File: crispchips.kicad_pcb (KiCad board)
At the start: 2 copper layers, 113 parts, among them IC1 ISL85003FRZ, IC2 ISL9307IRTAANFZ-T7A, IC3 ESP32-S2-MINI-1-N4R2, IC4 XC3S250E-4VQG100C, IC5 PCA9306DCUR, IC6 W25N512GVEIG, J2 Conn_01x02_Male, J3 Conn_01x04, J4 JTAG, J5 HDMI_A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

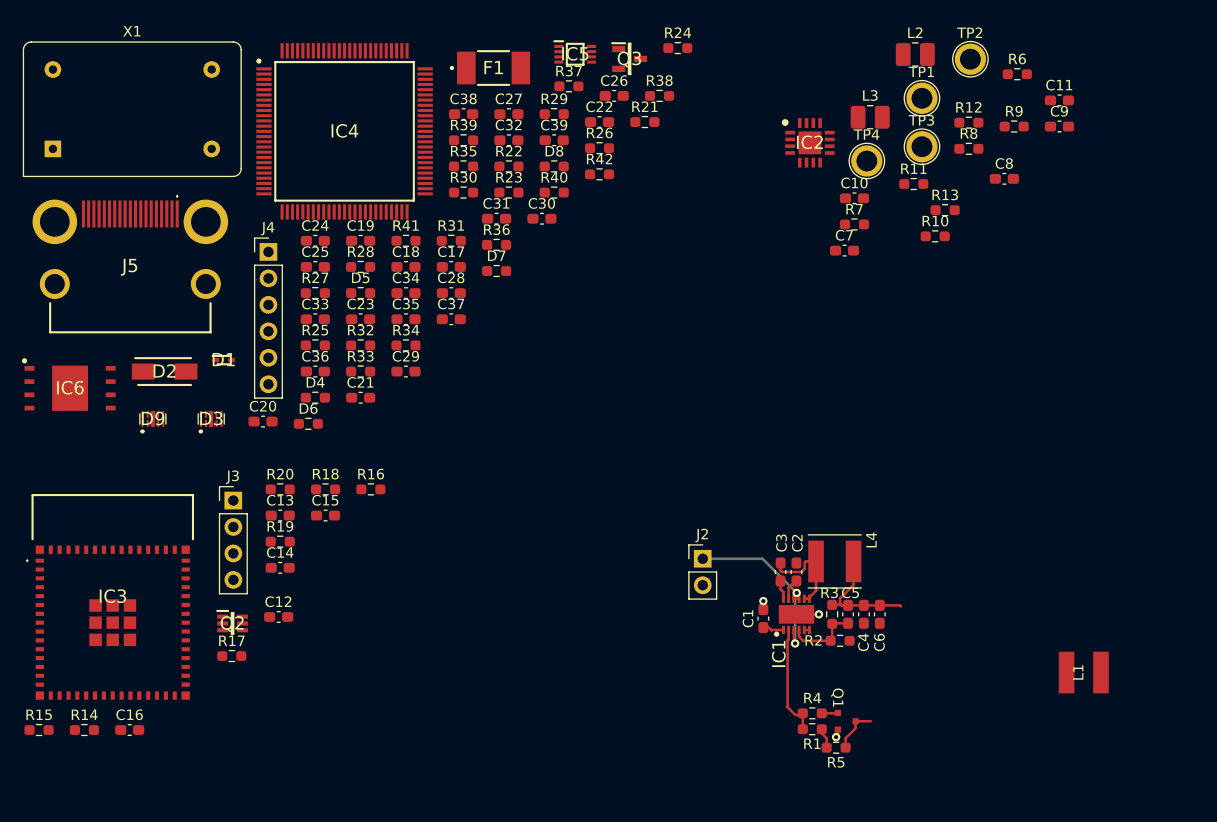
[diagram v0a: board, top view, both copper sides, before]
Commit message: supply layout review step
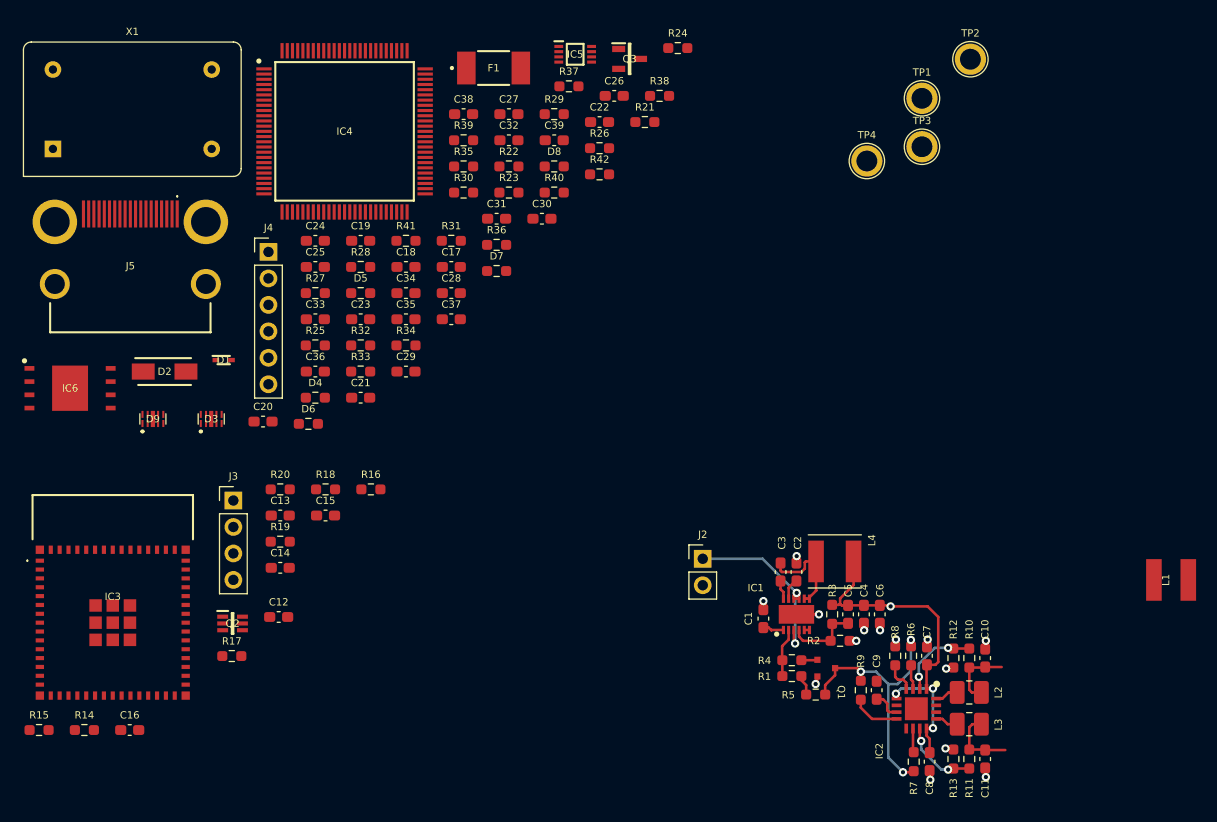
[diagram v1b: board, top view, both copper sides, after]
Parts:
- moved C11 63.6 mm to (201.6, 127.9), turned to -90 degrees
- moved L2 61.5 mm to (200.1, 121.5)
- moved L3 59.0 mm to (200.1, 124.6)
- moved C9 56.9 mm to (191.2, 121.3), turned to 90 degrees
- moved R6 56.8 mm to (194.5, 118.0), turned to -90 degrees
- moved C8 56.4 mm to (196.3, 128.2), turned to -90 degrees
- moved R9 56.1 mm to (189.7, 121.3), turned to -90 degrees
- moved R11 55.4 mm to (200.1, 127.9), turned to -90 degrees
- moved IC2 55.3 mm to (195.0, 123.1), turned to -90 degrees
- moved R13 52.7 mm to (198.6, 127.9), turned to 90 degrees
- moved R7 51.9 mm to (194.8, 128.2), turned to 90 degrees
- moved R12 51.4 mm to (198.6, 118.2), turned to -90 degrees
- moved R8 49.2 mm to (193.0, 118.0), turned to -90 degrees
- moved C10 45.9 mm to (201.6, 118.2), turned to 90 degrees
- moved R10 40.6 mm to (200.1, 118.2), turned to 90 degrees
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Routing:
- net ISL_5V: track 13.3 -> 36.9 mm, vias 0 -> 4
- net PG: track 4.42 -> 25.9 mm, vias 0 -> 3
- net GND: track 4.27 -> 12.9 mm, vias 3 -> 14
- net Net-(IC2-Pad2): track 0.00 -> 8.30 mm, vias 0 -> 2
- net Net-(IC2-Pad11): track 0.00 -> 7.52 mm, vias 0 -> 2
- net ISL_1V2: track 0.00 -> 6.90 mm
- net ISL_3V3: track 0.00 -> 6.60 mm
- net ISL8500_PG: track 10.8 -> 4.69 mm
- net Net-(IC2-Pad8): track 0.00 -> 4.64 mm
- net ISL_2V5_LDO: track 0.00 -> 2.81 mm
- net Net-(IC2-Pad4): track 0.00 -> 2.49 mm
- net Net-(IC2-Pad16): track 0.00 -> 2.32 mm
- net Net-(IC2-Pad10): track 0.00 -> 2.30 mm
- net Net-(IC2-Pad13): track 0.00 -> 2.23 mm
- net Net-(IC2-Pad3): track 0.00 -> 1.84 mm

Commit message: supply routing
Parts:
- moved TP4 43.0 mm to (194.6, 113.3)
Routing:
- net ISL_5V: track 36.9 -> 37.2 mm, vias 4 -> 3
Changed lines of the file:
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@@
   )
   (footprint "TestPoint:TestPoint_Plated_Hole_D2.0mm" (layer "F.Cu")
-    (at 190.252 70.53)
+    (at 194.564 113.284)
     (descr "Plated Hole as test Point, diameter 2.0mm")
     (tags "test point plated hole")
@@
   (segment (start 187.5805 113.1335) (end 187.684 113.03) (width 0.25) (layer "F.Cu") (net 5))
   (segment (start 196.274195 125.9825) (end 196.274195 127.3245) (width 0.25) (layer "F.Cu") (net 5))
-  (segment (start 196.088 113.284) (end 192.532 113.284) (width 0.25) (layer "F.Cu") (net 5))
-  (segment (start 196.8325 118.8895) (end 197.104 118.618) (width 0.25) (layer "F.Cu") (net 5))
+  (segment (start 191.5945 113.284) (end 194.564 113.284) (width 0.25) (layer "F.Cu") (net 5))
   (segment (start 193.104195 122.132) (end 193.104195 121.730195) (width 0.25) (layer "F.Cu") (net 5))
   (segment (start 195.979195 125.007) (end 195.979195 125.6875) (width 0.25) (layer "F.Cu") (net 5))
@@
   (segment (start 195.979195 118.9305) (end 196.020195 118.8895) (width 0.25) (layer "F.Cu") (net 5))
   (segment (start 195.979195 121.207) (end 196.547 121.207) (width 0.25) (layer "F.Cu") (net 5))
-  (segment (start 192.4315 113.1835) (end 192.532 113.284) (width 0.25) (layer "F.Cu") (net 5))
   (segment (start 196.547 121.207) (end 196.596 121.158) (width 0.25) (layer "F.Cu") (net 5))
-  (segment (start 196.020195 118.8895) (end 196.8325 118.8895) (width 0.25) (layer "F.Cu") (net 5))
+  (segment (start 194.564 113.284) (end 196.596 113.284) (width 0.25) (layer "F.Cu") (net 5))
+  (segment (start 191.494 113.1835) (end 191.5945 113.284) (width 0.25) (layer "F.Cu") (net 5))
   (segment (start 186.922 113.1335) (end 187.5805 113.1335) (width 0.25) (layer "F.Cu") (net 5))
+  (segment (start 196.596 113.284) (end 197.104 113.792) (width 0.25) (layer "F.Cu") (net 5))
   (segment (start 184.4245 120.8365) (end 184.4245 121.749) (width 0.25) (layer "F.Cu") (net 5))
-  (segment (start 197.104 118.618) (end 197.104 114.3) (width 0.25) (layer "F.Cu") (net 5))
   (segment (start 193.104195 121.730195) (end 193.04 121.666) (width 0.25) (layer "F.Cu") (net 5))
   (segment (start 187.684 112.522) (end 188.976 111.23) (width 0.25) (layer "F.Cu") (net 5))
+  (segment (start 197.104 113.792) (end 197.104 118.618) (width 0.25) (layer "F.Cu") (net 5))
   (segment (start 183.9635 119.971) (end 183.9635 120.3755) (width 0.25) (layer "F.Cu") (net 5))
   (segment (start 183.9635 120.3755) (end 184.4245 120.8365) (width 0.25) (layer "F.Cu") (net 5))
+  (segment (start 197.104 118.618) (end 196.8325 118.8895) (width 0.25) (layer "F.Cu") (net 5))
   (segment (start 188.976 111.23) (end 188.976 108.966) (width 0.25) (layer "F.Cu") (net 5))
   (segment (start 195.979195 125.007) (end 196.557 125.007) (width 0.25) (layer "F.Cu") (net 5))
-  (segment (start 197.104 114.3) (end 196.088 113.284) (width 0.25) (layer "F.Cu") (net 5))
+  (segment (start 196.8325 118.8895) (end 196.020195 118.8895) (width 0.25) (layer "F.Cu") (net 5))
   (segment (start 187.8375 113.1835) (end 187.684 113.03) (width 0.25) (layer "F.Cu") (net 5))
   (segment (start 187.684 113.03) (end 187.684 112.522) (width 0.25) (layer "F.Cu") (net 5))
@@
   (segment (start 195.979195 125.6875) (end 196.274195 125.9825) (width 0.25) (layer "F.Cu") (net 5))
   (segment (start 195.979195 121.207) (end 195.979195 118.9305) (width 0.25) (layer "F.Cu") (net 5))
-  (segment (start 191.494 113.1835) (end 192.4315 113.1835) (width 0.25) (layer "F.Cu") (net 5))
   (via (at 196.596 121.158) (size 0.8) (drill 0.4) (layers "F.Cu" "B.Cu") (net 5))
   (via (at 193.04 121.666) (size 0.8) (drill 0.4) (layers "F.Cu" "B.Cu") (net 5))
-  (via (at 192.532 113.284) (size 0.8) (drill 0.4) (layers "F.Cu" "B.Cu") (net 5))
   (via (at 196.596 124.968) (size 0.8) (drill 0.4) (layers "F.Cu" "B.Cu") (net 5))
   (segment (start 196.596 124.968) (end 196.596 121.158) (width 0.25) (layer "B.Cu") (net 5))
@@
   (via (at 183.366 116.84) (size 0.8) (drill 0.4) (layers "F.Cu" "B.Cu") (net 28))
   (segment (start 183.366 116.84) (end 183.366 112.134418) (width 0.25) (layer "B.Cu") (net 28))
-  (segment (start 183.515563 111.984855) (end 180.242708 108.712) (width 0.25) (layer "B.Cu") (net 28))
-  (segment (start 180.242708 108.712) (end 174.498 108.712) (width 0.25) (layer "B.Cu") (net 28))
+  (segment (start 183.515563 111.555209) (end 180.672354 108.712) (width 0.25) (layer "B.Cu") (net 28))
+  (segment (start 183.515563 111.984855) (end 183.515563 111.555209) (width 0.25) (layer "B.Cu") (net 28))
+  (segment (start 180.672354 108.712) (end 174.498 108.712) (width 0.25) (layer "B.Cu") (net 28))
   (segment (start 183.366 112.134418) (end 183.515563 111.984855) (width 0.25) (layer "B.Cu") (net 28))
   (segment (start 195.243 120.041) (end 195.329195 120.127195) (width 0.25) (layer "F.Cu") (net 29))

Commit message: added test points
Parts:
- moved TP1 63.5 mm to (205.2, 127.3)
- moved TP2 62.6 mm to (205.2, 123.2)
- moved TP3 50.9 mm to (205.2, 119.1)
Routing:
- net ISL_2V5_LDO: track 2.81 -> 19.8 mm, vias 0 -> 1
- net ISL_5V: track 37.2 -> 43.3 mm
- net PG: track 25.9 -> 28.2 mm
- net ISL_3V3: track 6.60 -> 8.65 mm
- net ISL_1V2: track 6.90 -> 8.72 mm
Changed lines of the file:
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@@
   )
   (footprint "TestPoint:TestPoint_Plated_Hole_D2.0mm" (layer "F.Cu")
-    (at 200.192 60.76)
+    (at 205.232 123.19)
     (descr "Plated Hole as test Point, diameter 2.0mm")
     (tags "test point plated hole")
@@
   )
   (footprint "TestPoint:TestPoint_Plated_Hole_D2.0mm" (layer "F.Cu")
-    (at 195.542 64.51)
+    (at 205.232 127.254)
     (descr "Plated Hole as test Point, diameter 2.0mm")
     (tags "test point plated hole")
@@
   )
   (footprint "TestPoint:TestPoint_Plated_Hole_D2.0mm" (layer "F.Cu")
-    (at 195.542 69.16)
+    (at 205.232 119.126)
     (descr "Plated Hole as test Point, diameter 2.0mm")
     (tags "test point plated hole")
@@
   (segment (start 196.274195 125.9825) (end 196.274195 127.3245) (width 0.25) (layer "F.Cu") (net 5))
   (segment (start 191.5945 113.284) (end 194.564 113.284) (width 0.25) (layer "F.Cu") (net 5))
+  (segment (start 197.104 113.792) (end 203.2 113.792) (width 0.25) (layer "F.Cu") (net 5))
   (segment (start 193.104195 122.132) (end 193.104195 121.730195) (width 0.25) (layer "F.Cu") (net 5))
   (segment (start 195.979195 125.007) (end 195.979195 125.6875) (width 0.25) (layer "F.Cu") (net 5))
@@
   (segment (start 192.210195 122.599) (end 191.802695 122.1915) (width 0.25) (layer "F.Cu") (net 7))
   (segment (start 191.802695 122.1915) (end 191.194195 122.1915) (width 0.25) (layer "F.Cu") (net 7))
+  (segment (start 191.262 122.936) (end 191.194195 122.868195) (width 0.25) (layer "F.Cu") (net 7))
+  (segment (start 191.194195 122.868195) (end 191.194195 122.1915) (width 0.25) (layer "F.Cu") (net 7))
   (segment (start 192.379195 123.432) (end 192.210195 123.263) (width 0.25) (layer "F.Cu") (net 7))
+  (via (at 191.262 122.936) (size 0.8) (drill 0.4) (layers "F.Cu" "B.Cu") (net 7))
+  (segment (start 196.088 125.73) (end 200.406 125.73) (width 0.25) (layer "B.Cu") (net 7))
+  (segment (start 200.406 125.73) (end 202.946 123.19) (width 0.25) (layer "B.Cu") (net 7))
+  (segment (start 193.294 122.936) (end 196.088 125.73) (width 0.25) (layer "B.Cu") (net 7))
+  (segment (start 202.946 123.19) (end 205.232 123.19) (width 0.25) (layer "B.Cu") (net 7))
+  (segment (start 191.262 122.936) (end 193.294 122.936) (width 0.25) (layer "B.Cu") (net 7))
+  (segment (start 205.2085 119.1025) (end 201.608195 119.1025) (width 0.25) (layer "F.Cu") (net 8))
   (segment (start 200.084195 119.1525) (end 200.084195 121.288) (width 0.25) (layer "F.Cu") (net 8))
   (segment (start 200.084195 119.1525) (end 201.558195 119.1525) (width 0.25) (layer "F.Cu") (net 8))
+  (segment (start 205.232 119.126) (end 205.2085 119.1025) (width 0.25) (layer "F.Cu") (net 8))
   (segment (start 200.134195 119.1025) (end 200.084195 119.1525) (width 0.25) (layer "F.Cu") (net 8))
   (segment (start 201.558195 119.1525) (end 201.608195 119.1025) (width 0.25) (layer "F.Cu") (net 8))
-  (segment (start 201.608195 119.1025) (end 203.191695 119.1025) (width 0.25) (layer "F.Cu") (net 8))
   (segment (start 200.084195 121.288) (end 200.338195 121.542) (width 0.25) (layer "F.Cu") (net 8))
   (segment (start 200.338195 121.542) (end 201.246695 121.542) (width 0.25) (layer "F.Cu") (net 8))
@@
   (segment (start 201.558195 127.0205) (end 201.608195 127.0705) (width 0.25) (layer "F.Cu") (net 9))
   (segment (start 201.246695 124.59) (end 200.379195 124.59) (width 0.25) (layer "F.Cu") (net 9))
-  (segment (start 201.608195 127.0705) (end 203.539695 127.0705) (width 0.25) (layer "F.Cu") (net 9))
+  (segment (start 204.978 127) (end 201.678695 127) (width 0.25) (layer "F.Cu") (net 9))
+  (segment (start 205.232 127.254) (end 204.978 127) (width 0.25) (layer "F.Cu") (net 9))
+  (segment (start 201.678695 127) (end 201.608195 127.0705) (width 0.25) (layer "F.Cu") (net 9))
   (segment (start 200.084195 127.0205) (end 201.558195 127.0205) (width 0.25) (layer "F.Cu") (net 9))
   (segment (start 182.118 117.094) (end 182.118 118.4265) (width 0.25) (layer "F.Cu") (net 27))
@@
   (segment (start 185.465 118.447) (end 185.503 118.409) (width 0.25) (layer "F.Cu") (net 142))
   (segment (start 183.9635 118.447) (end 185.465 118.447) (width 0.25) (layer "F.Cu") (net 142))
+  (segment (start 194.056 129.032) (end 194.1235 129.0995) (width 0.25) (layer "F.Cu") (net 143))
+  (segment (start 194.056 129.032) (end 194.056 128.27) (width 0.25) (layer "F.Cu") (net 143))
   (segment (start 189.328195 119.209) (end 187.203 119.209) (width 0.25) (layer "F.Cu") (net 143))
-  (segment (start 194.646695 129.203) (end 194.750195 129.0995) (width 0.25) (layer "F.Cu") (net 143))
+  (segment (start 188.722 120.65) (end 188.9555 120.4165) (width 0.25) (layer "F.Cu") (net 143))
+  (segment (start 194.1235 129.0995) (end 194.750195 129.0995) (width 0.25) (layer "F.Cu") (net 143))
   (segment (start 194.481 116.503) (end 194.481 117.099305) (width 0.25) (layer "F.Cu") (net 143))
+  (segment (start 188.9555 120.4165) (end 189.670195 120.4165) (width 0.25) (layer "F.Cu") (net 143))
   (segment (start 187.203 119.883) (end 186.2495 120.8365) (width 0.25) (layer "F.Cu") (net 143))
   (segment (start 189.670195 119.551) (end 189.670195 120.4165) (width 0.25) (layer "F.Cu") (net 143))
   (segment (start 186.2495 120.8365) (end 186.2495 121.749) (width 0.25) (layer "F.Cu") (net 143))
-  (segment (start 193.719 129.203) (end 194.646695 129.203) (width 0.25) (layer "F.Cu") (net 143))
+  (segment (start 188.722 122.936) (end 188.722 120.65) (width 0.25) (layer "F.Cu") (net 143))
   (segment (start 194.481 117.099305) (end 194.496195 117.1145) (width 0.25) (layer "F.Cu") (net 143))
+  (segment (start 194.056 128.27) (end 188.722 122.936) (width 0.25) (layer "F.Cu") (net 143))
   (segment (start 187.203 119.209) (end 187.203 119.883) (width 0.25) (layer "F.Cu") (net 143))
   (segment (start 189.670195 119.551) (end 189.328195 119.209) (width 0.25) (layer "F.Cu") (net 143))
   (via (at 194.481 116.503) (size 0.8) (drill 0.4) (layers "F.Cu" "B.Cu") (net 143))
   (via (at 189.670195 119.551) (size 0.8) (drill 0.4) (layers "F.Cu" "B.Cu") (net 143))
-  (via (at 193.719 129.203) (size 0.8) (drill 0.4) (layers "F.Cu" "B.Cu") (net 143))
+  (via (at 194.056 129.032) (size 0.8) (drill 0.4) (layers "F.Cu" "B.Cu") (net 143))
   (segment (start 189.670195 119.551) (end 191.126978 119.551) (width 0.25) (layer "B.Cu") (net 143))
-  (segment (start 193.719 129.203) (end 192.315489 127.799489) (width 0.25) (layer "B.Cu") (net 143))
-  (segment (start 192.315489 127.799489) (end 192.315489 120.739511) (width 0.25) (layer "B.Cu") (net 143))
   (segment (start 191.126978 119.551) (end 192.315489 120.739511) (width 0.25) (layer "B.Cu") (net 143))
   (segment (start 193.204489 120.739511) (end 192.315489 120.739511) (width 0.25) (layer "B.Cu") (net 143))

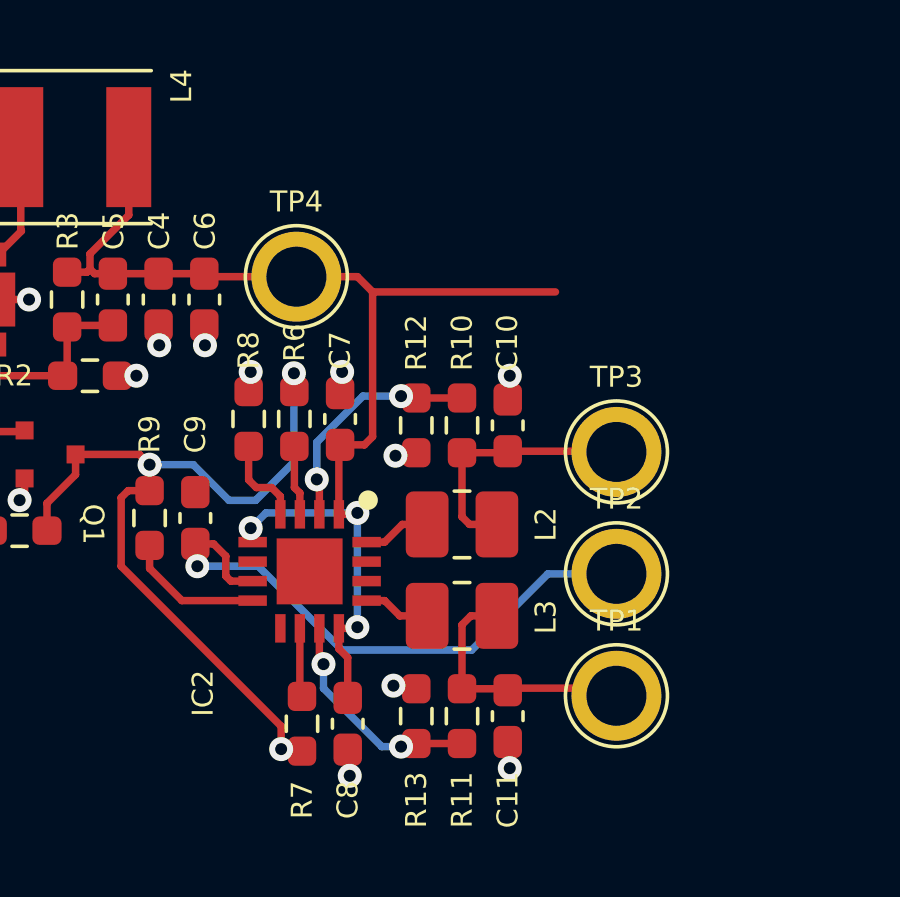
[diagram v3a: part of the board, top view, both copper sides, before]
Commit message: changed testpoint footprints
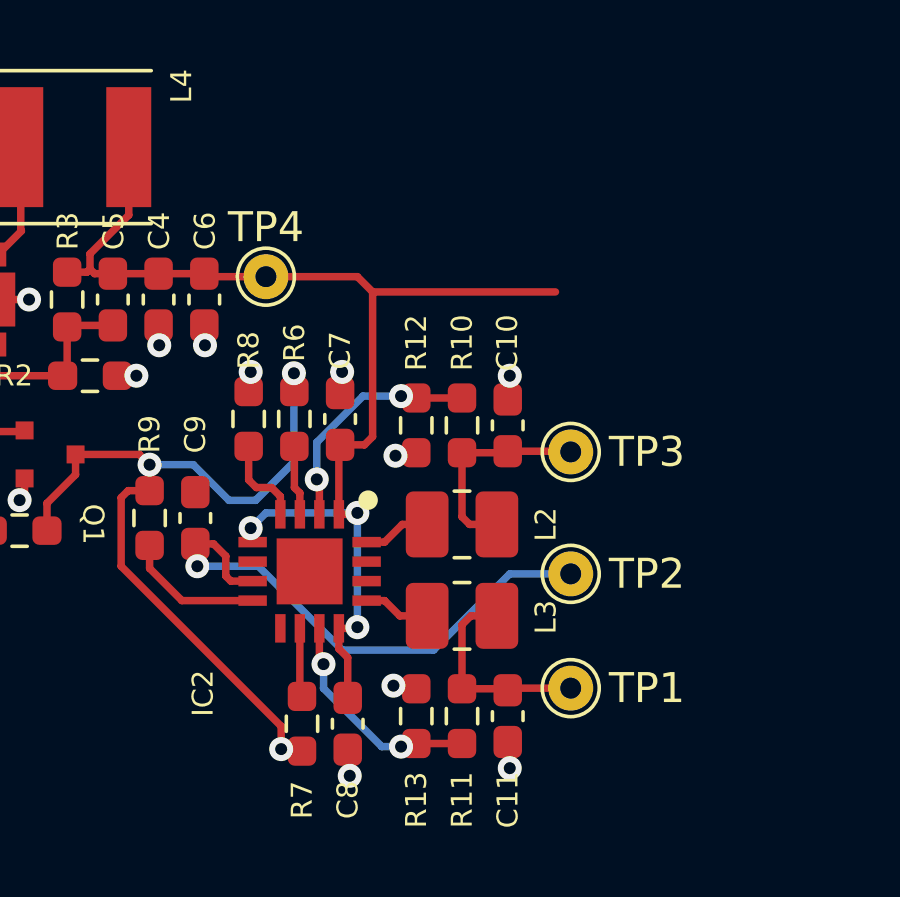
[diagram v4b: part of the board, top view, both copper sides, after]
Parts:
- TP1, TP2, TP3, TP4: footprint TestPoint:TestPoint_Plated_Hole_D2.0mm -> TestPoint:TestPoint_THTPad_D1.5mm_Drill0.7mm
- moved TP1 1.55 mm to (203.7, 127.0)
- moved TP2 1.52 mm to (203.7, 123.2)
- moved TP3 1.52 mm to (203.7, 119.1)
- moved TP4 1.02 mm to (193.5, 113.3)
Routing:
- net ISL_1V2: track 8.72 -> 7.09 mm
- net ISL_2V5_LDO: track 19.8 -> 18.2 mm
- net ISL_3V3: track 8.65 -> 7.13 mm

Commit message: supply rerouting
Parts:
- moved TP4 4.06 mm to (197.6, 113.3)
- moved C11 1.32 mm to (202.2, 126.7)
- moved C8 1.32 mm to (196.8, 127.0)
- moved R11 1.32 mm to (200.7, 126.7)
- moved R13 1.32 mm to (199.1, 126.7)
- moved R7 1.32 mm to (195.3, 127.0)
- moved TP3 1.32 mm to (204.3, 117.9)
- moved C10 1.32 mm to (202.2, 117.1)
- moved C7 1.32 mm to (196.6, 116.8)
- moved C9 1.32 mm to (191.8, 120.1)
- moved IC2 1.32 mm to (195.6, 121.9)
- moved L2 1.32 mm to (200.7, 120.4)
- moved L3 1.32 mm to (200.7, 123.4)
- moved R10 1.32 mm to (200.7, 117.1)
- moved R12 1.32 mm to (199.1, 117.1)
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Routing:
- net PG: track 28.2 -> 25.7 mm, vias 3 -> 0
- net ISL_5V: track 43.3 -> 42.0 mm
